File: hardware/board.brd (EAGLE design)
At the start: 53 x 30 mm, 45 parts, among them IC1 0915BM15A0001, J1 U.FL, U3 BLE113-A, X1 24MHz 8pF 10ppm -20C +70C, X3 MINI-USB-UX60-MB-5ST

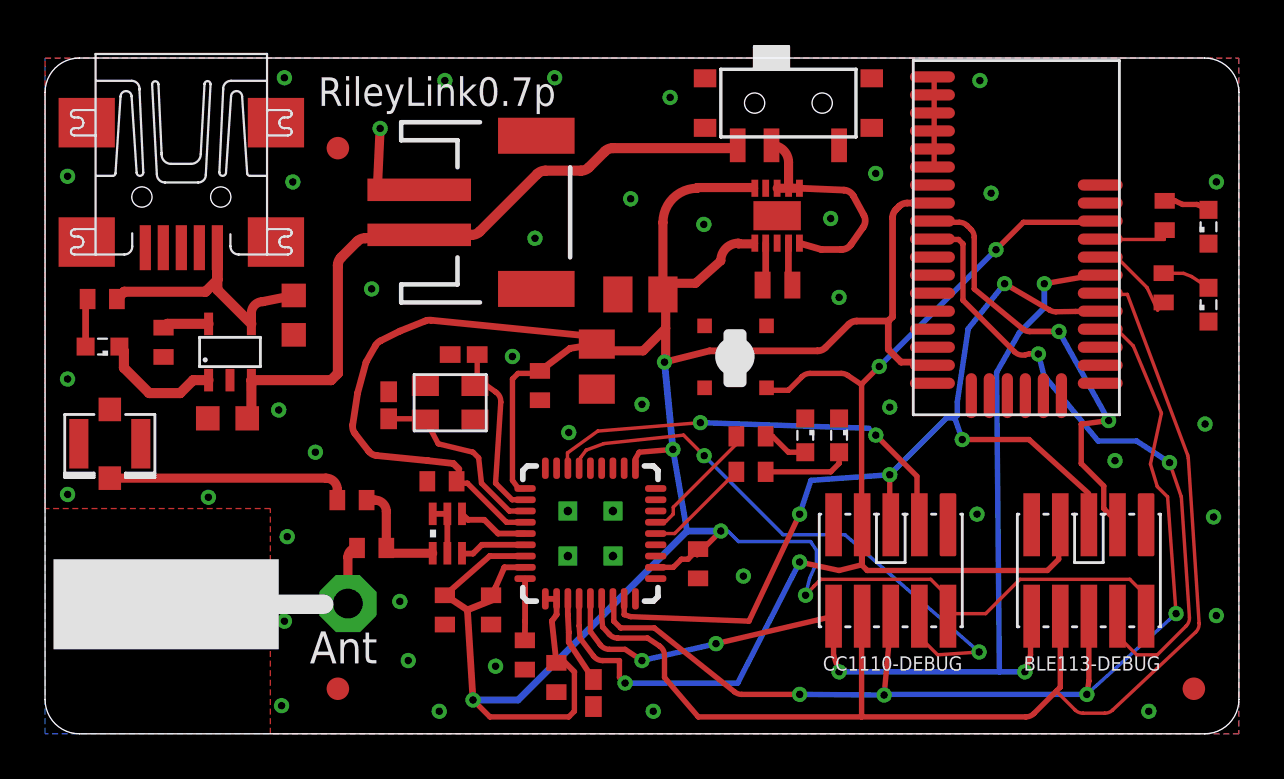
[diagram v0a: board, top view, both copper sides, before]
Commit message: Experiment: fix antenna test point
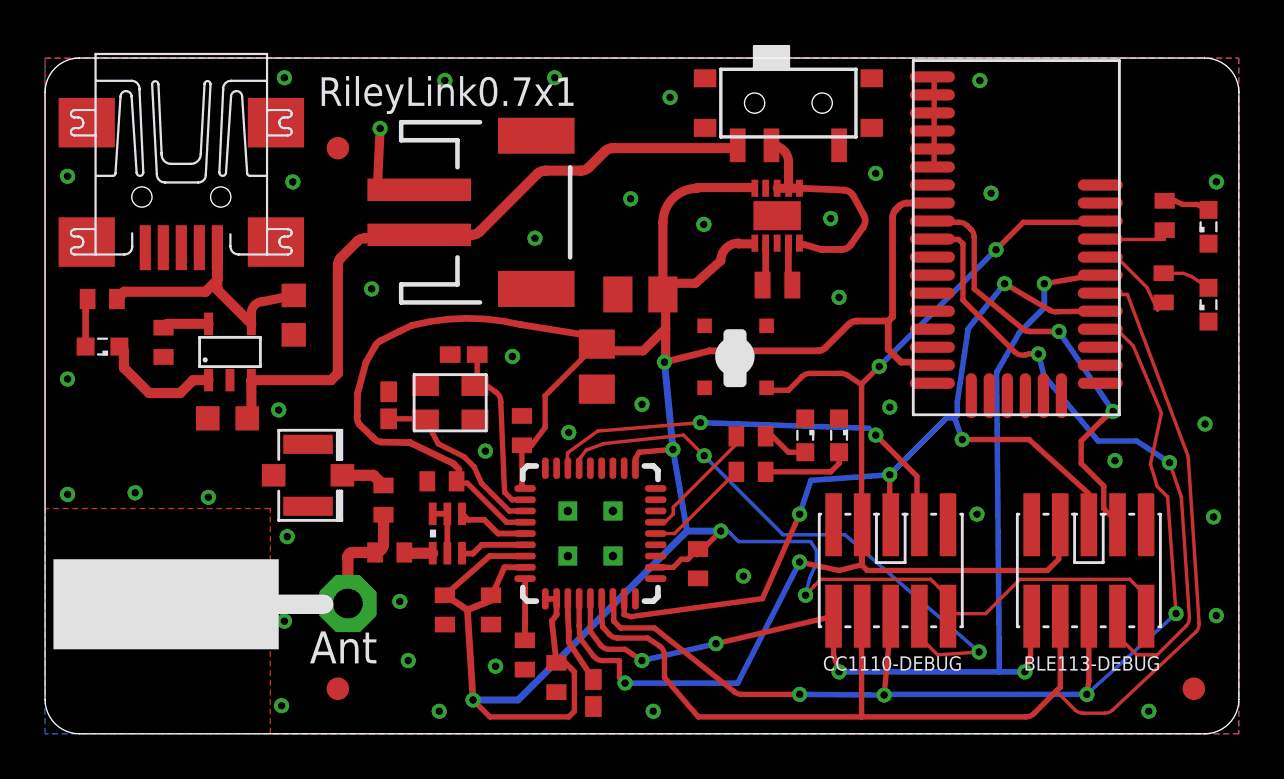
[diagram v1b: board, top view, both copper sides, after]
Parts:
- moved J1 8.91 mm to (11.7, 11.5), turned to 0 degrees
- moved C12 2.15 mm to (21.2, 13.5), turned to 90 degrees
- moved R4 1.40 mm to (15.0, 10.4), turned to 270 degrees
- moved R9 0.82 mm to (15.3, 8.05)
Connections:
- net N$10: no longer R4.2
- net N$12: now also R4.2
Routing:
- net N$9: track 10.8 -> 2.01 mm
- net N$10: track 4.94 -> 1.35 mm
- net N$12: track 2.64 -> 5.19 mm
- net VDD: track 151.7 -> 150.0 mm
- net SSN: track 44.5 -> 44.0 mm
- net GND: vias 41 -> 42
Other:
- board text added: "RileyLink0.7x1"
- board text removed: "RileyLink0.7p"
